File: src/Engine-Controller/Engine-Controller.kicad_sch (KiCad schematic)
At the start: 14 parts, among them J1 Jumper_NO, J2 Jumper_NO, U1 STM32H750VBTx

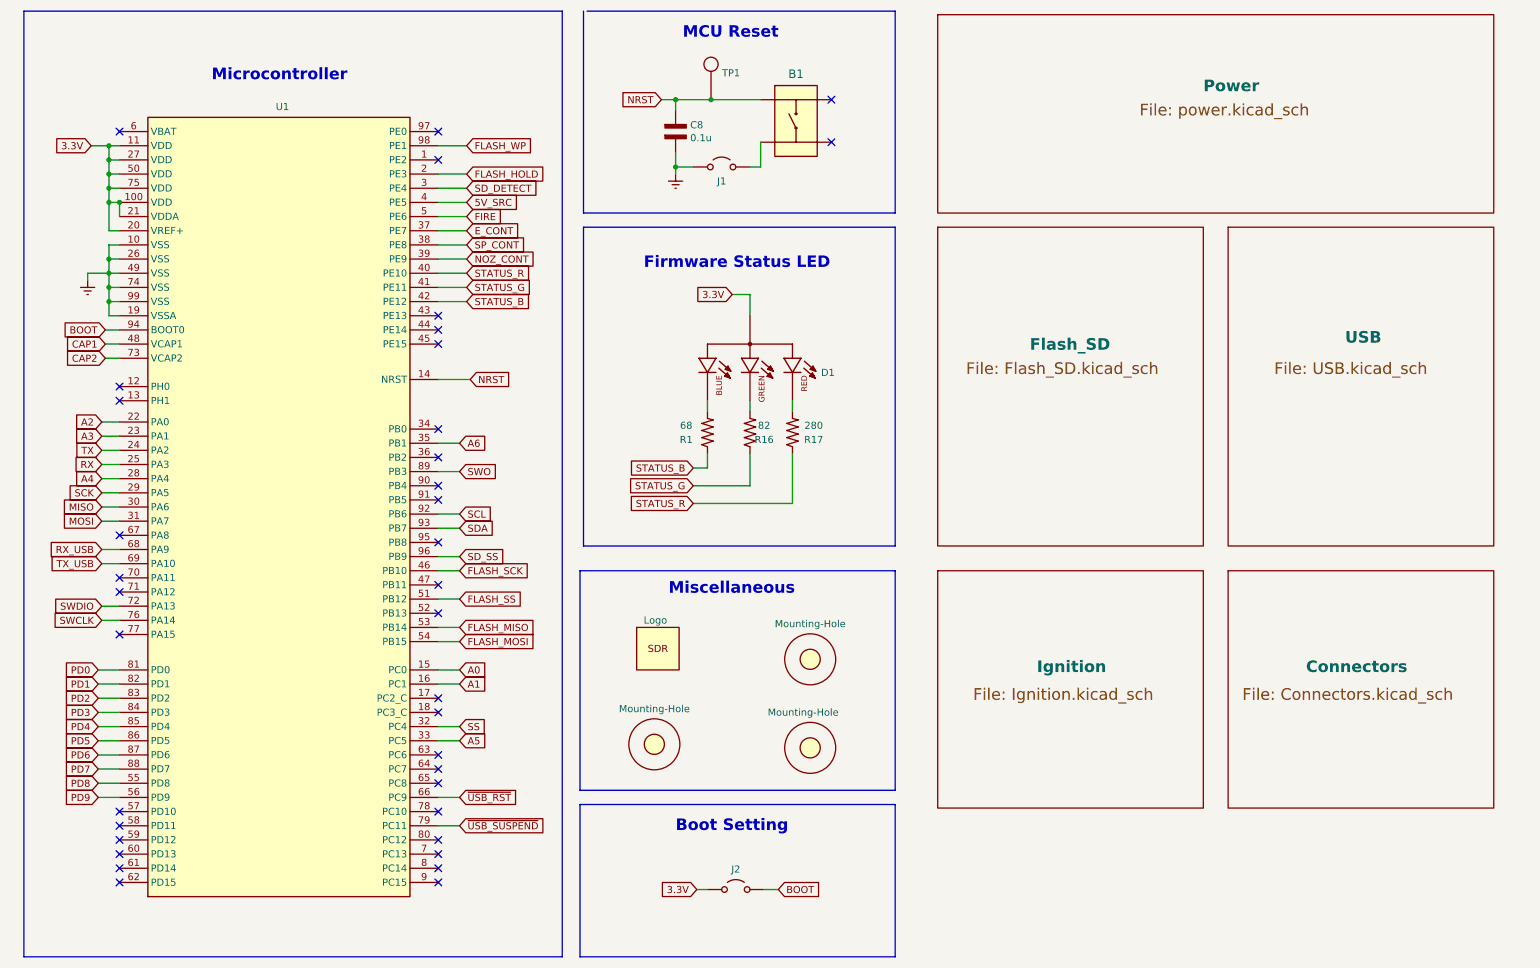
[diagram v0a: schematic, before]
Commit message: merged all non power components into single sheet
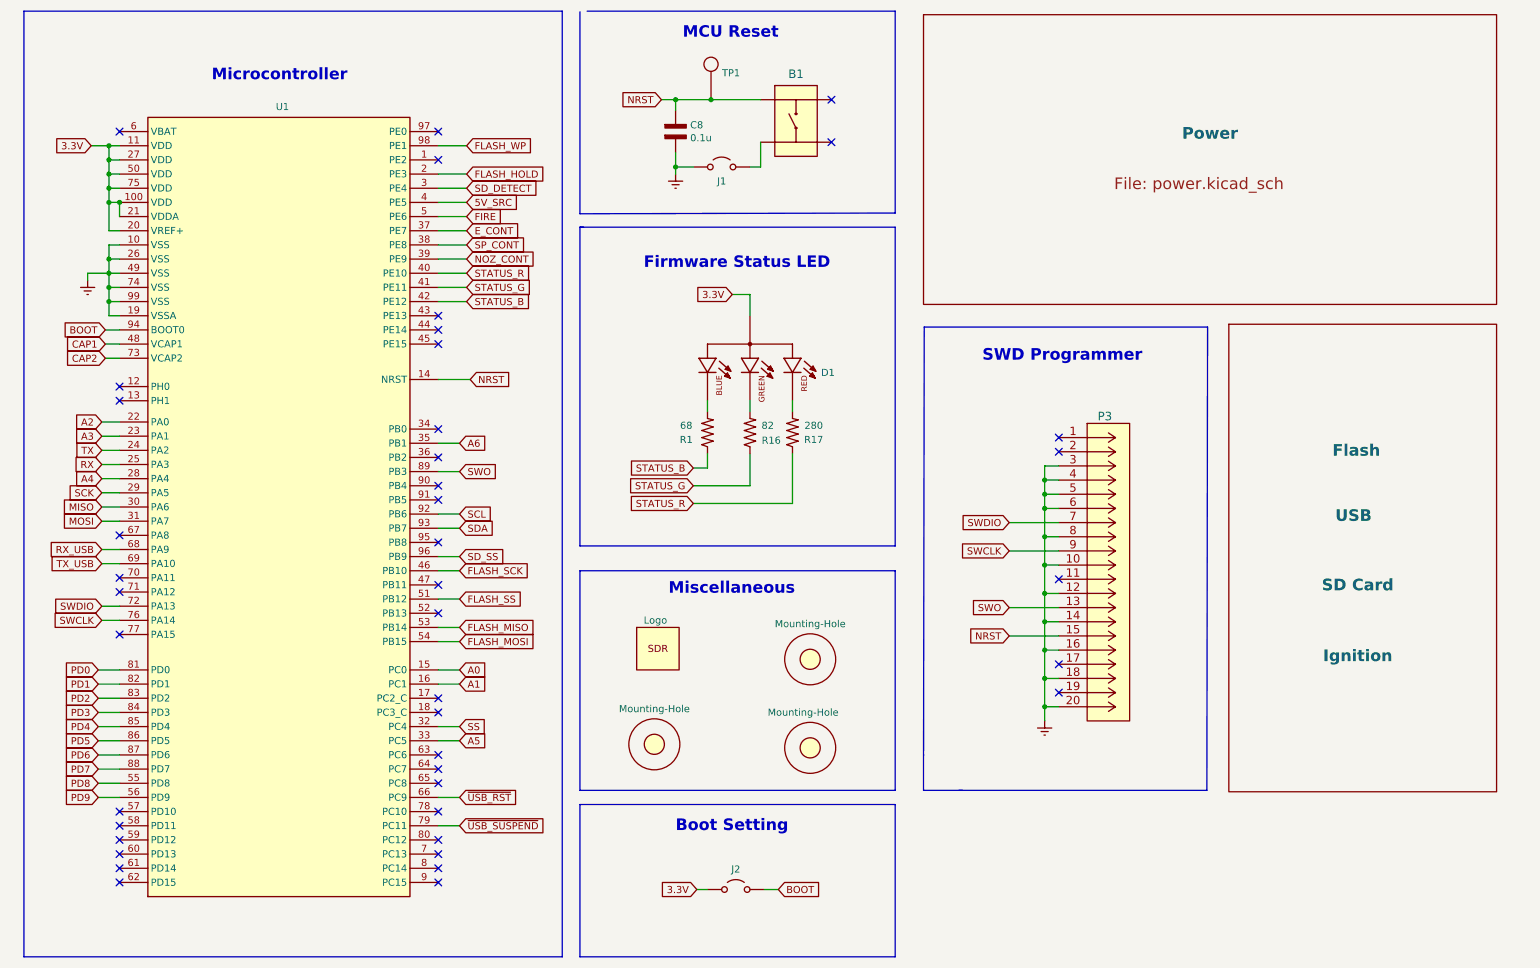
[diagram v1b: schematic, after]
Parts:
- added P3: SBH11-PBPC-D10-RA-BK, CONN20_D10-RA-BK_SUL, symbol Engine-Controller:SBH11-PBPC-D10-RA-BK
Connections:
- net Earth: now also P3.10, P3.12, P3.14, P3.16, P3.18, P3.20, P3.3, P3.4, P3.5, P3.6, P3.8
- net NRST: now also P3.15
- net SWCLK: now also P3.9
- net SWDIO: now also P3.7
- net SWO: now also P3.13
- no-connect marks 37 -> 42
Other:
- removed sheet Connectors
- removed sheet Flash_SD
- removed sheet Ignition
- removed sheet USB
- added sheet Page2 (Page2.kicad_sch)
- note added: "SWD Programmer"

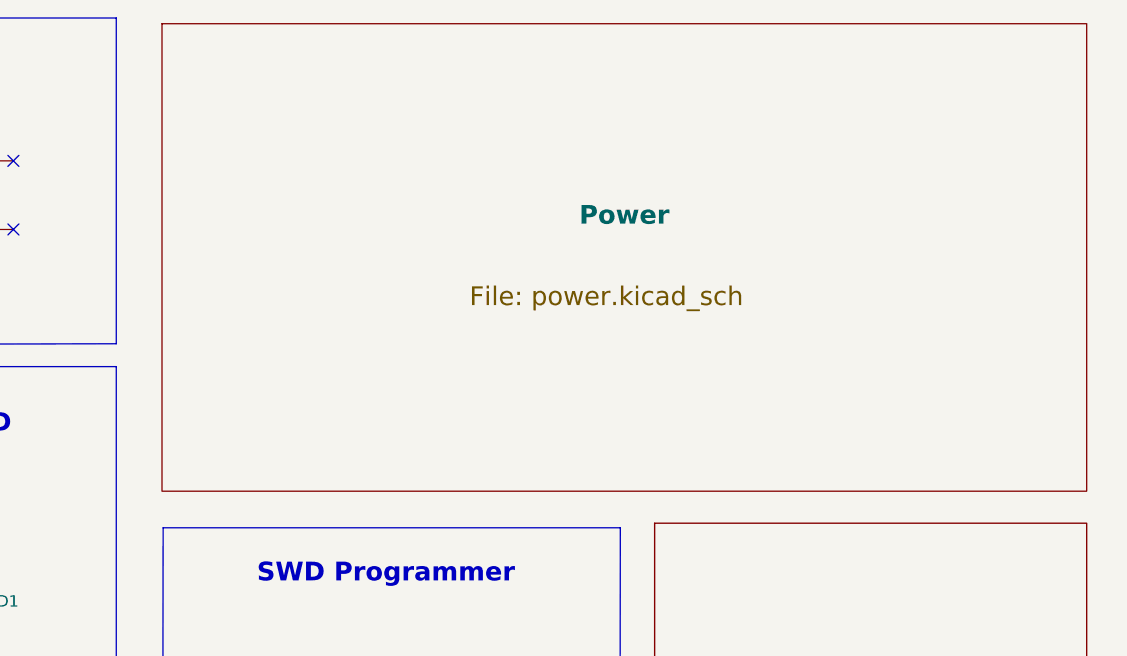
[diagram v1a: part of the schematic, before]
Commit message: added new sheet for sensor interfaces
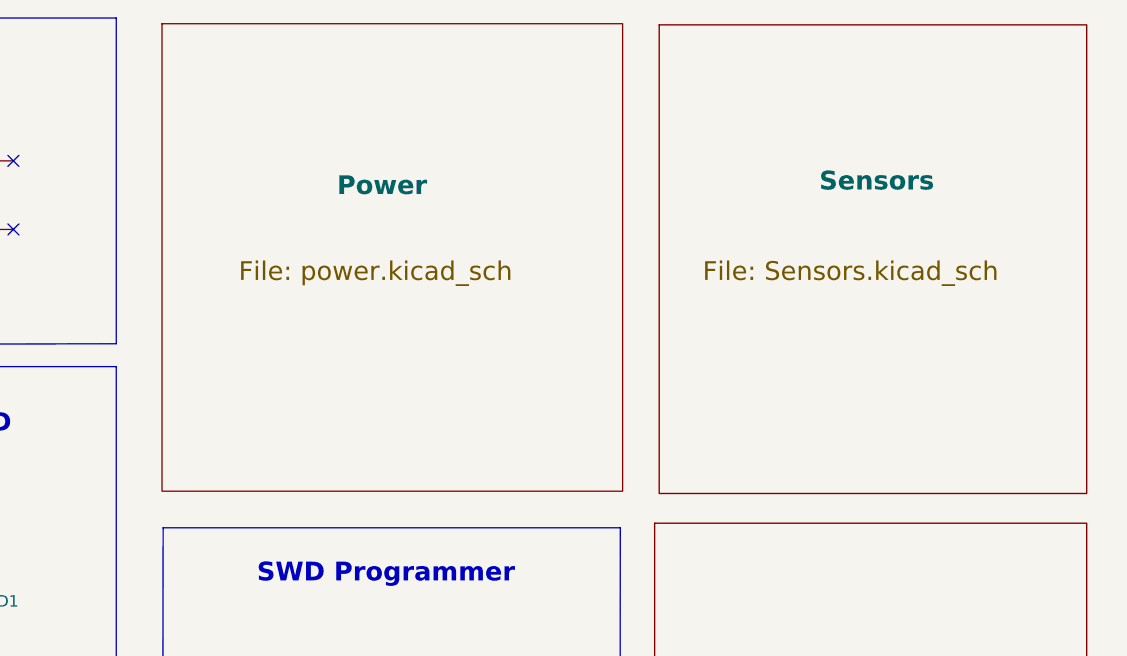
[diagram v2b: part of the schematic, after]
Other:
- added sheet Sensors (Sensors.kicad_sch)
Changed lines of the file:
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@@
     )
   )
-  (sheet (at 177.165 20.955) (size 102.743 51.943)
+  (sheet (at 177.165 20.955) (size 51.181 51.943)
     (stroke (width 0) (type solid) (color 0 0 0 0))
     (fill (color 0 0 0 0.0000))
-    (property "Sheet name" "Power" (id 0) (at 223.52 43.434 0)
+    (property "Sheet name" "Power" (id 0) (at 196.596 40.132 0)
       (effects (font (size 2.08 2.08) bold) (justify left bottom))
     )
-    (property "Sheet file" "power.kicad_sch" (id 1) (at 211.328 50.038 0)
+    (property "Sheet file" "power.kicad_sch" (id 1) (at 185.674 47.244 0)
       (effects (font (size 2.08 2.08)) (justify left top))
     )
@@
     )
   )
+  (sheet (at 232.41 21.082) (size 47.498 52.07)
+    (stroke (width 0.1524) (type solid) (color 0 0 0 0))
+    (fill (color 0 0 0 0.0000))
+    (property "Sheet name" "Sensors" (id 0) (at 250.19 39.624 0)
+      (effects (font (size 2.08 2.08) bold) (justify left bottom))
+    )
+    (property "Sheet file" "Sensors.kicad_sch" (id 1) (at 237.236 47.244 0)
+      (effects (font (size 2.08 2.08)) (justify left top))
+    )
+  )
   (sheet_instances
     (path "/" (page "1"))
+    (path "/d060135e-4b32-4403-ae1a-9301174376e1" (page "4"))
     (path "/00000000-0000-0000-0000-000060d7f309" (page "6"))
     (path "/9f3f32e1-1873-42fa-9cca-aa278e3c01ec" (page "6"))

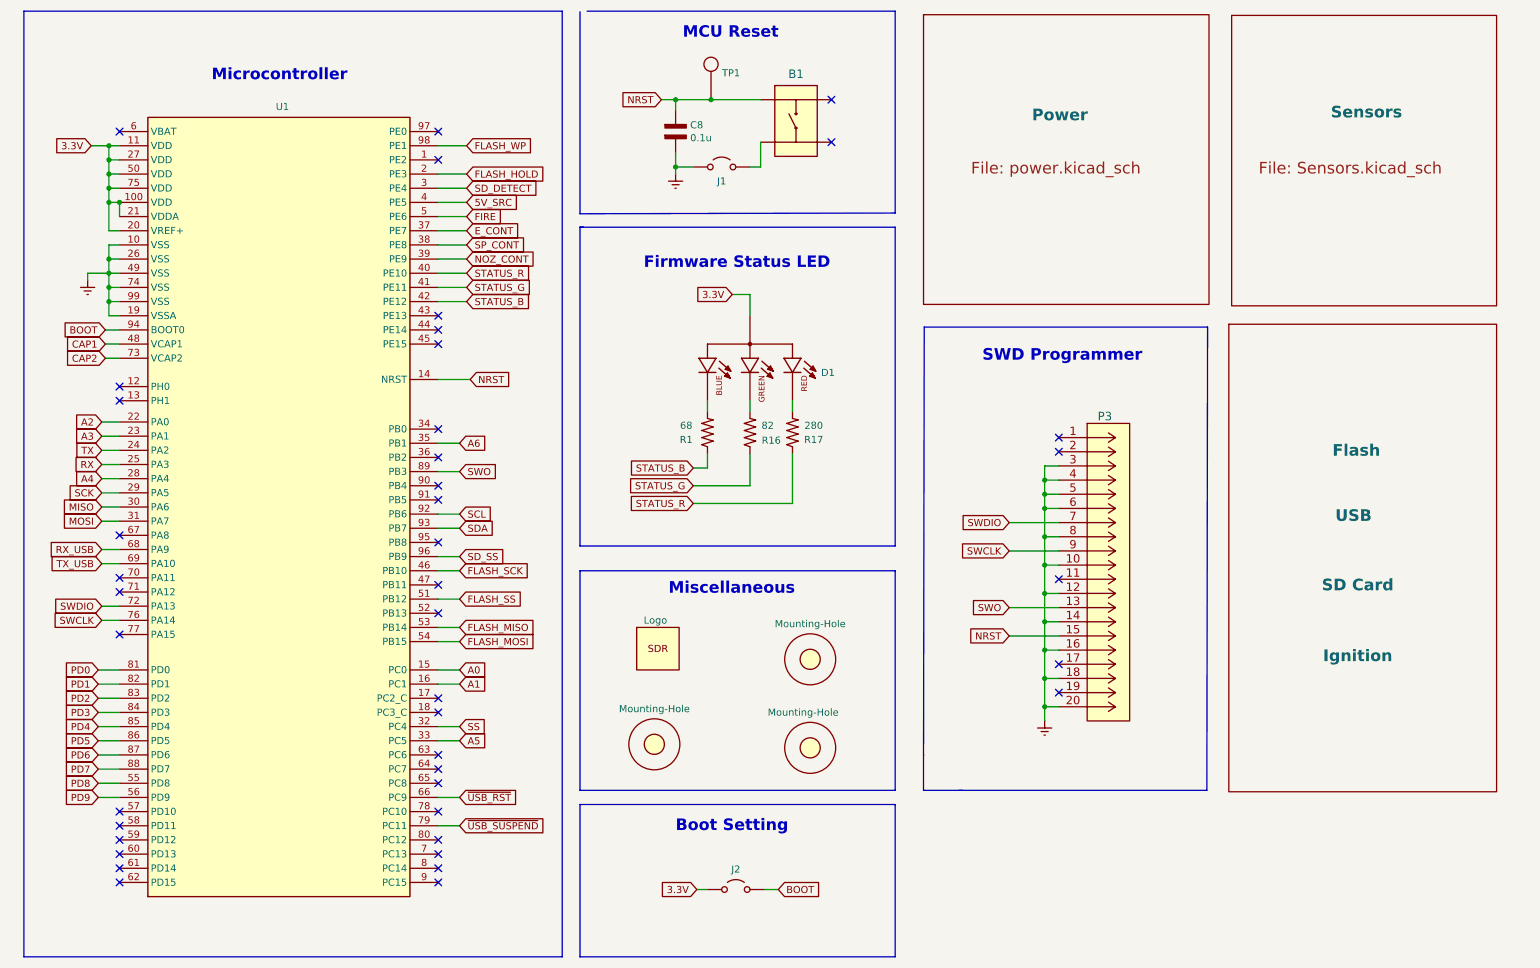
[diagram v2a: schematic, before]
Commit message: updated SWD connector
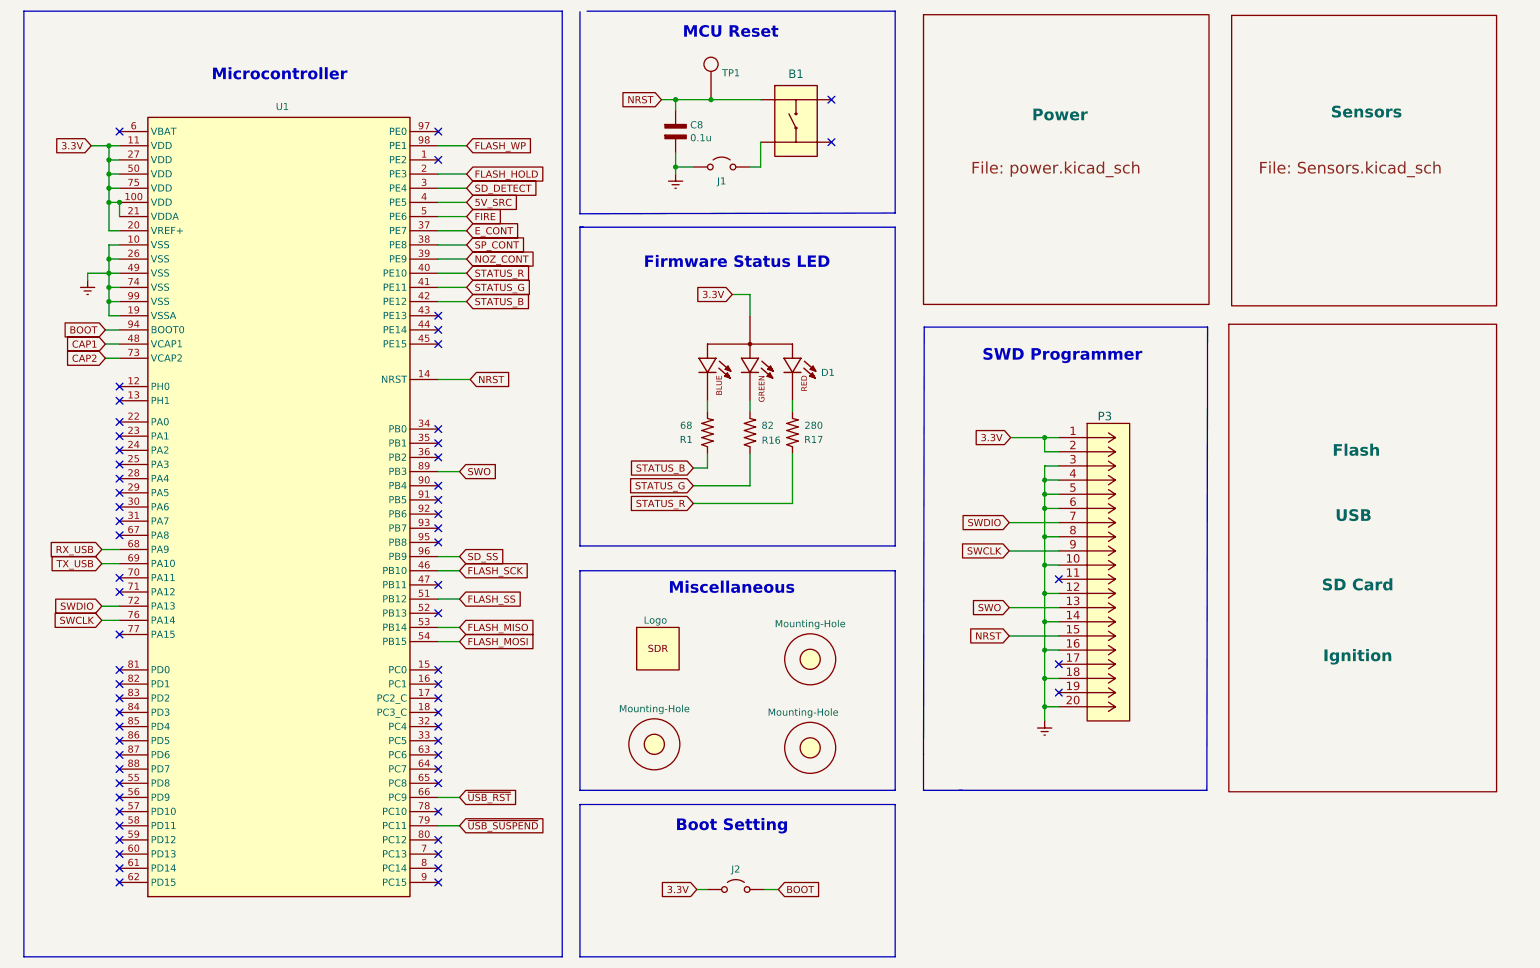
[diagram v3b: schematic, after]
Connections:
- net 3.3V: now also P3.1, P3.2
- net A0: no longer names the net of U1.15 (PC0)
- net A1: no longer names the net of U1.16 (PC1)
- net A2: no longer names the net of U1.22 (PA0)
- net A3: no longer names the net of U1.23 (PA1)
- net A4: no longer names the net of U1.28 (PA4)
- net A5: no longer names the net of U1.33 (PC5)
- net A6: no longer names the net of U1.35 (PB1)
- net MISO: no longer names the net of U1.30 (PA6)
- net MOSI: no longer names the net of U1.31 (PA7)
- net PD0: no longer names the net of U1.81 (PD0)
- net PD1: no longer names the net of U1.82 (PD1)
- net PD2: no longer names the net of U1.83 (PD2)
- net PD3: no longer names the net of U1.84 (PD3)
- net PD4: no longer names the net of U1.85 (PD4)
- net PD5: no longer names the net of U1.86 (PD5)
- net PD6: no longer names the net of U1.87 (PD6)
- net PD7: no longer names the net of U1.88 (PD7)
- net PD8: no longer names the net of U1.55 (PD8)
- net PD9: no longer names the net of U1.56 (PD9)
- net RX: no longer names the net of U1.25 (PA3)
- net SCK: no longer names the net of U1.29 (PA5)
- net SCL: no longer names the net of U1.92 (PB6)
- net SDA: no longer names the net of U1.93 (PB7)
- net SS: no longer names the net of U1.32 (PC4)
- net TX: no longer names the net of U1.24 (PA2)
- no-connect marks 42 -> 65

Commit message: Added connectors for valve controller and main power line
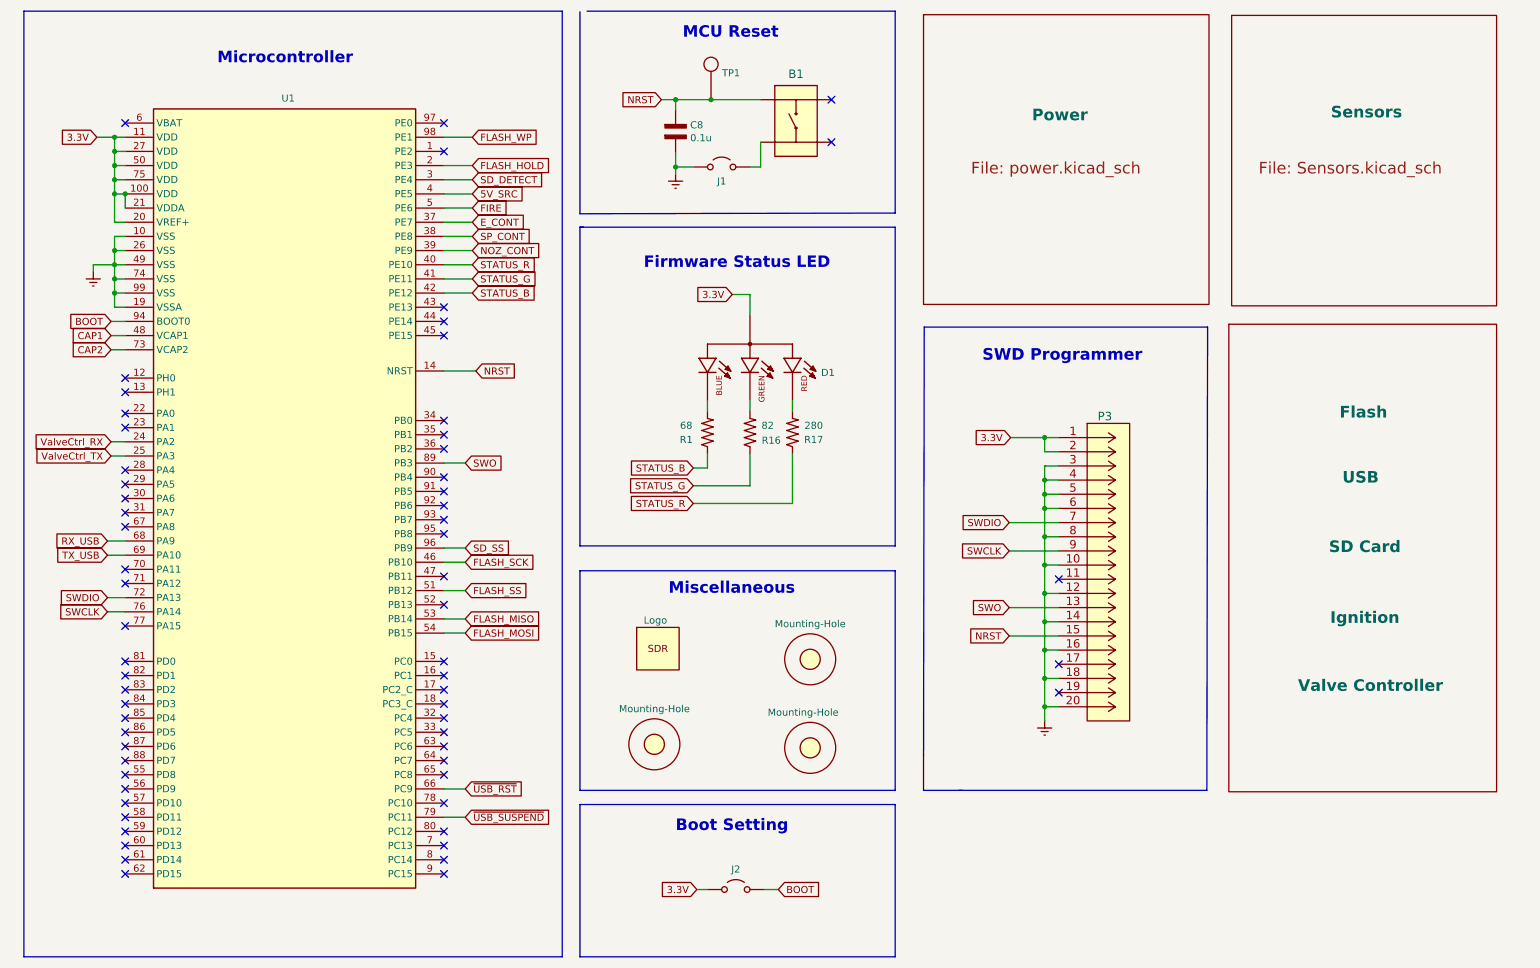
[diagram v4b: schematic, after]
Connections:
- net ValveCtrl_RX: now reaches U1.24 (PA2)
- net ValveCtrl_TX: now reaches U1.25 (PA3)
- no-connect marks 65 -> 63
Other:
- moved on the sheet: U1
